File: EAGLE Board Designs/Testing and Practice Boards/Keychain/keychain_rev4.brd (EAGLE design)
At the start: 27.9 x 27.9 mm, 14 parts, among them J1 USB4110, U1 LM555

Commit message: update
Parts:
- R3: value RESISTOR_0603_60.4 -> RESISTOR_0603_10
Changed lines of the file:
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@@
 <drawing>
 <settings>
-<setting alwaysvectorfont="yes"/>
+<setting alwaysvectorfont="no"/>
 <setting verticaltext="up"/>
 </settings>
@@
 <attribute name="VOLTAGE_MAX" value="200V" x="-5.334" y="39.624" size="1.778" layer="28" rot="MR90" display="off"/>
 </element>
-<element name="R3" library="HyTechDevices" package="0603-RES" value="RESISTOR_0603_60.4" x="15.748" y="11.684" smashed="yes" rot="MR90">
-<attribute name="DKPN" value="311-60.4HRCT-ND" x="-5.842" y="26.924" size="1.778" layer="28" rot="MR90" display="off"/>
+<element name="R3" library="HyTechDevices" package="0603-RES" value="RESISTOR_0603_10" x="15.748" y="11.684" smashed="yes" rot="MR90">
+<attribute name="DKPN" value="311-10.0HRCT-ND" x="-5.842" y="26.924" size="1.778" layer="28" rot="MR90" display="off"/>
 <attribute name="MANUFACTURER" value="Yageo" x="-5.842" y="26.924" size="1.778" layer="28" rot="MR90" display="off"/>
-<attribute name="MOPN" value="603-RC0603FR-0760R4L" x="-5.842" y="26.924" size="1.778" layer="28" rot="MR90" display="off"/>
-<attribute name="MPN" value="RC0603FR-0760R4L" x="-5.842" y="26.924" size="1.778" layer="28" rot="MR90" display="off"/>
+<attribute name="MOPN" value="603-RC0603FR-0710RL" x="-5.842" y="26.924" size="1.778" layer="28" rot="MR90" display="off"/>
+<attribute name="MPN" value="RC0603FR-0710RL" x="-5.842" y="26.924" size="1.778" layer="28" rot="MR90" display="off"/>
 <attribute name="NAME" x="16.383" y="11.684" size="0.8128" layer="26" font="vector" rot="MR90" align="bottom-center"/>
 <attribute name="POWER" value="0.1W" x="-5.842" y="26.924" size="1.778" layer="28" rot="MR90" display="off"/>
-<attribute name="RESISTANCE" value="60.4" x="-5.842" y="26.924" size="1.778" layer="28" rot="MR90" display="off"/>
+<attribute name="RESISTANCE" value="10" x="-5.842" y="26.924" size="1.778" layer="28" rot="MR90" display="off"/>
 <attribute name="TOLERANCE" value="1%" x="-5.842" y="26.924" size="1.778" layer="28" rot="MR90" display="off"/>
-<attribute name="VOLTAGE_CONTINUOUS" value="2.48V" x="-5.842" y="26.924" size="1.778" layer="28" rot="MR90" display="off"/>
+<attribute name="VOLTAGE_CONTINUOUS" value="1.00V" x="-5.842" y="26.924" size="1.778" layer="28" rot="MR90" display="off"/>
 <attribute name="VOLTAGE_MAX" value="75V" x="-5.842" y="26.924" size="1.778" layer="28" rot="MR90" display="off"/>
 </element>

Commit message: Fixed Shayan's bad work
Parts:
- turned D1 to 270 degrees
- turned D2 to 180 degrees
- turned D3 to 0 degrees
- turned D4 to 90 degrees
- turned D5 to 180 degrees
- turned D6 to 0 degrees
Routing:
- net N$2: track 42.0 -> 11.3 mm, vias 2 -> 0
- net N$3: track 19.3 -> 0.00 mm, vias 2 -> 0
- net GND: track 6.14 -> 8.56 mm, vias 0 -> 1
- added copper zone on layer 1, net GND
- added copper zone on layer 1, net N$3
- removed copper zone on layer 16, net GND

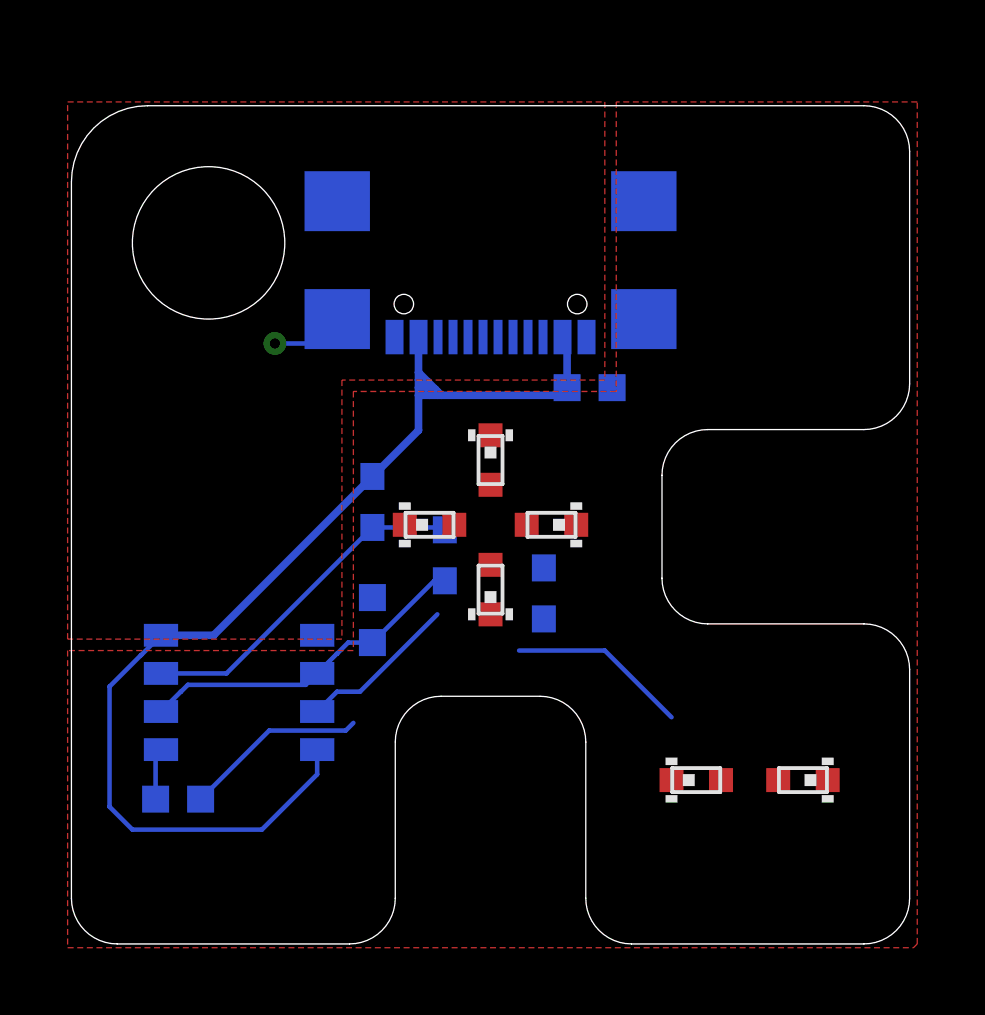
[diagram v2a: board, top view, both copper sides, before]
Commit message: Added some routes
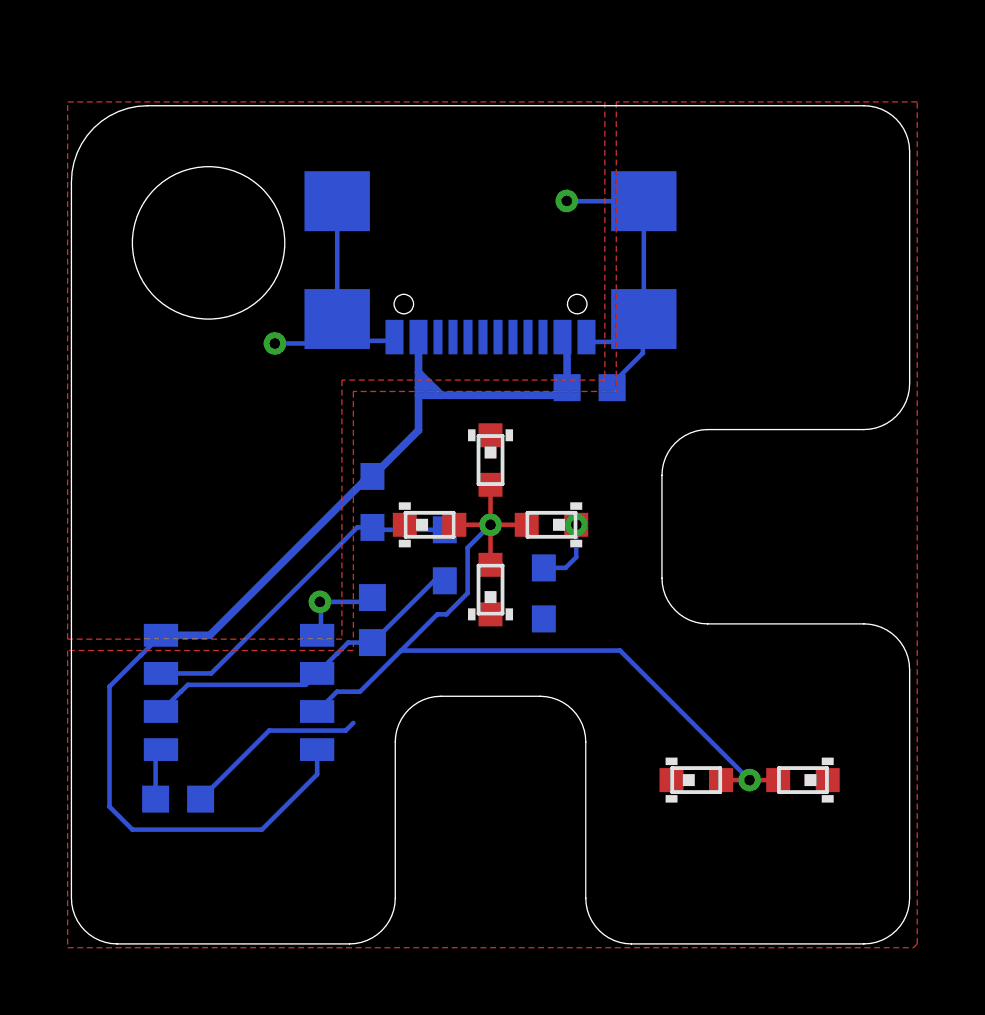
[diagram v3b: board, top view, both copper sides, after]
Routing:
- net GND: track 8.56 -> 27.6 mm, vias 1 -> 3
- net N$2: track 11.3 -> 29.6 mm, vias 0 -> 2
- net N$3: track 0.00 -> 2.31 mm, vias 0 -> 1
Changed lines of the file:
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@@
 <drawing>
 <settings>
-<setting alwaysvectorfont="yes"/>
+<setting alwaysvectorfont="no"/>
 <setting verticaltext="up"/>
 </settings>
@@
 <vertex x="9.652" y="18.288"/>
 <vertex x="9.652" y="12.954"/>
-<vertex x="10.414" y="12.954"/>
-<vertex x="10.414" y="14.986"/>
+<vertex x="10.287" y="12.954"/>
+<vertex x="10.287" y="14.986"/>
 <vertex x="12.954" y="14.986"/>
 <vertex x="12.954" y="17.78"/>
@@
 <wire x1="8.0466" y1="20.0146" x2="6.7824" y2="20.0146" width="0.1524" layer="16"/>
 <via x="6.7824" y="20.0146" extent="1-16" drill="0.35"/>
-<wire x1="19.08" y1="20.828" x2="19.08" y2="24.758" width="0" layer="19" extent="16-16"/>
-<wire x1="17.17" y1="20.228" x2="19.08" y2="20.828" width="0" layer="19" extent="16-16"/>
-<wire x1="18.022" y1="18.542" x2="17.17" y2="20.228" width="0" layer="19" extent="16-16"/>
-<wire x1="8.86" y1="20.828" x2="10.77" y2="20.228" width="0" layer="19" extent="16-16"/>
-<wire x1="8.86" y1="24.758" x2="8.86" y2="20.828" width="0" layer="19" extent="16-16"/>
-<wire x1="15.748" y1="10.834" x2="18.022" y2="18.542" width="0" layer="19" extent="16-16"/>
+<wire x1="8.3185" y1="11.3665" x2="8.3185" y2="10.414" width="0.1524" layer="16"/>
+<wire x1="8.1915" y1="10.287" x2="8.3185" y2="10.414" width="0.1524" layer="16"/>
+<wire x1="8.283575" y1="11.401425" x2="8.3185" y2="11.3665" width="0.1524" layer="16"/>
+<via x="8.283575" y="11.401425" extent="1-16" drill="0.35"/>
+<wire x1="10.033" y1="11.545" x2="9.889425" y2="11.401425" width="0.1524" layer="16"/>
+<wire x1="9.889425" y1="11.401425" x2="8.283575" y2="11.401425" width="0.1524" layer="16"/>
+<wire x1="8.86" y1="24.758" x2="8.86" y2="20.828" width="0.1524" layer="16"/>
+<wire x1="10.77" y1="20.228" x2="10.643" y2="20.101" width="0.1524" layer="16"/>
+<wire x1="10.643" y1="20.101" x2="9.363" y2="20.101" width="0.1524" layer="16"/>
+<wire x1="9.363" y1="20.101" x2="9.144" y2="20.32" width="0.1524" layer="16"/>
+<wire x1="19.08" y1="24.758" x2="16.517" y2="24.758" width="0.1524" layer="16"/>
+<wire x1="16.517" y1="24.758" x2="16.51" y2="24.765" width="0.1524" layer="16"/>
+<via x="16.51" y="24.765" extent="1-16" drill="0.35"/>
+<wire x1="19.08" y1="24.758" x2="19.08" y2="20.828" width="0.1524" layer="16"/>
+<wire x1="17.332" y1="20.066" x2="17.17" y2="20.228" width="0.1524" layer="16"/>
+<wire x1="19.05" y1="20.066" x2="17.332" y2="20.066" width="0.1524" layer="16"/>
+<wire x1="19.05" y1="19.697" x2="18.022" y2="18.669" width="0.1524" layer="16"/>
+<wire x1="18.022" y1="18.542" x2="18.022" y2="18.669" width="0.1524" layer="16"/>
+<wire x1="19.05" y1="19.697" x2="19.05" y2="20.066" width="0.1524" layer="16"/>
 <wire x1="10.033" y1="11.545" x2="15.748" y2="10.834" width="0" layer="19" extent="16-16"/>
-<wire x1="8.1915" y1="10.287" x2="10.033" y2="11.545" width="0" layer="19" extent="16-16"/>
+<wire x1="9.144" y1="20.32" x2="8.86" y2="20.828" width="0" layer="19" extent="16-16"/>
 <wire x1="9.398" y1="7.366" x2="8.1915" y2="10.287" width="0" layer="19" extent="16-16"/>
 </signal>
@@
 <wire x1="11.811" y1="18.415" x2="11.684" y2="18.542" width="0.254" layer="16"/>
 <wire x1="11.684" y1="18.542" x2="11.57" y2="18.542" width="0.254" layer="16"/>
-<wire x1="10.033" y1="15.582" x2="4.738" y2="10.287" width="0.254" layer="16"/>
-<wire x1="4.738" y1="10.287" x2="2.9845" y2="10.287" width="0.254" layer="16"/>
+<wire x1="10.033" y1="15.582" x2="9.906" y2="15.582" width="0.254" layer="16"/>
+<wire x1="9.906" y1="15.582" x2="4.611" y2="10.287" width="0.254" layer="16"/>
+<wire x1="4.611" y1="10.287" x2="2.9845" y2="10.287" width="0.254" layer="16"/>
 <wire x1="2.9845" y1="10.287" x2="2.3241" y2="9.6266" width="0.1524" layer="16"/>
 <wire x1="2.3241" y1="9.6266" x2="2.3183125" y2="9.6266" width="0.1524" layer="16"/>
@@
 <vertex x="9.398" y="9.779"/>
 </polygon>
-<wire x1="16.827" y1="13.97" x2="15.748" y2="12.534" width="0" layer="19" extent="1-16"/>
+<via x="16.827" y="13.97" extent="1-16" drill="0.35"/>
+<wire x1="16.827" y1="13.97" x2="16.827" y2="12.89" width="0.1524" layer="16"/>
+<wire x1="16.471" y1="12.534" x2="15.748" y2="12.534" width="0.1524" layer="16"/>
+<wire x1="16.827" y1="12.89" x2="16.471" y2="12.534" width="0.1524" layer="16"/>
 </signal>
 <signal name="N$6">
@@
 <contactref element="R1" pad="1"/>
 <contactref element="R2" pad="2"/>
-<wire x1="10.033" y1="13.882" x2="12.368" y2="13.882" width="0.1524" layer="16"/>
-<wire x1="12.368" y1="13.882" x2="12.446" y2="13.804" width="0.1524" layer="16"/>
-<wire x1="10.033" y1="13.882" x2="5.168" y2="9.017" width="0.1524" layer="16"/>
-<wire x1="5.168" y1="9.017" x2="2.9845" y2="9.017" width="0.1524" layer="16"/>
+<wire x1="10.033" y1="13.882" x2="9.525" y2="13.882" width="0.1524" layer="16"/>
+<wire x1="9.525" y1="13.882" x2="4.66" y2="9.017" width="0.1524" layer="16"/>
+<wire x1="4.66" y1="9.017" x2="2.9845" y2="9.017" width="0.1524" layer="16"/>
+<wire x1="12.446" y1="13.804" x2="10.111" y2="13.804" width="0.1524" layer="16"/>
+<wire x1="10.111" y1="13.804" x2="10.033" y2="13.882" width="0.1524" layer="16"/>
 </signal>
 <signal name="N$2">
@@
 <wire x1="8.1915" y1="7.747" x2="8.8519" y2="8.4074" width="0.1524" layer="16"/>
 <wire x1="8.8519" y1="8.4074" x2="9.6186875" y2="8.4074" width="0.1524" layer="16"/>
-<wire x1="9.6186875" y1="8.4074" x2="12.1972875" y2="10.986" width="0.1524" layer="16"/>
-<wire x1="14.923" y1="9.779" x2="17.78" y2="9.779" width="0.1524" layer="16"/>
-<wire x1="17.78" y1="9.779" x2="20.003" y2="7.556" width="0.1524" layer="16"/>
-<wire x1="15.177" y1="13.97" x2="13.97" y2="15.304" width="0" layer="19" extent="1-1"/>
-<wire x1="12.763" y1="13.97" x2="13.97" y2="15.304" width="0" layer="19" extent="1-1"/>
-<wire x1="13.97" y1="12.636" x2="15.177" y2="13.97" width="0" layer="19" extent="1-1"/>
-<wire x1="12.1972875" y1="10.986" x2="13.97" y2="12.636" width="0" layer="19" extent="1-16"/>
-<wire x1="14.923" y1="9.779" x2="12.1972875" y2="10.986" width="0" layer="19" extent="16-16"/>
-<wire x1="21.653" y1="5.461" x2="20.003" y2="7.556" width="0" layer="19" extent="1-16"/>
-<wire x1="21.653" y1="5.461" x2="23.559" y2="5.461" width="0" layer="19" extent="1-1"/>
+<wire x1="12.1972875" y1="10.986" x2="10.9902875" y2="9.779" width="0.1524" layer="16"/>
+<wire x1="10.95614375" y1="9.74485625" x2="9.6186875" y2="8.4074" width="0.1524" layer="16"/>
+<wire x1="12.763" y1="13.97" x2="13.97" y2="13.97" width="0.1524" layer="1"/>
+<via x="13.97" y="13.97" extent="1-16" drill="0.35"/>
+<wire x1="15.177" y1="13.97" x2="13.97" y2="13.97" width="0.1524" layer="1"/>
+<wire x1="13.97" y1="15.304" x2="13.97" y2="13.97" width="0.1524" layer="1"/>
+<wire x1="13.97" y1="12.636" x2="13.97" y2="13.97" width="0.1524" layer="1"/>
+<wire x1="21.653" y1="5.461" x2="22.606" y2="5.461" width="0.1524" layer="1"/>
+<via x="22.606" y="5.461" extent="1-16" drill="0.35"/>
+<wire x1="23.559" y1="5.461" x2="22.606" y2="5.461" width="0.1524" layer="1"/>
+<wire x1="13.97" y1="13.97" x2="13.208" y2="13.208" width="0.1524" layer="16"/>
+<wire x1="10.9902875" y1="9.779" x2="10.95614375" y2="9.74485625" width="0.1524" layer="16"/>
+<wire x1="22.606" y1="5.461" x2="18.288" y2="9.779" width="0.1524" layer="16"/>
+<wire x1="18.288" y1="9.779" x2="10.9902875" y2="9.779" width="0.1524" layer="16"/>
+<wire x1="13.208" y1="13.208" x2="13.208" y2="11.6927125" width="0.1524" layer="16"/>
+<wire x1="13.208" y1="11.6927125" x2="12.5012875" y2="10.986" width="0.1524" layer="16"/>
+<wire x1="12.5012875" y1="10.986" x2="12.1972875" y2="10.986" width="0.1524" layer="16"/>
 </signal>
 </signals>
